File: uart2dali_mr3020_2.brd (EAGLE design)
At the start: 52 x 70 mm, 79 parts, among them IC2 LM393D, IC3 SFH6156, IC4 SFH6156, J1 AVR_SPI_PRG_6NS, Q1 SST201, Q2 BSP170P, Q3 BC817-25SMD, X1 SM04B-SRSS-TB

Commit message: - added values parts of constant current circuit - dali master can query from slaves
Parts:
- D5: value BZX84CSMD -> BZX84CSMD3v3
- D6: value BZX84CSMD -> BZX84CSMD12V
- R13: value (none) -> 3k9
- R14: value (none) -> 33k
- R15, R17, R18: value (none) -> 2k2
- R16: value (none) -> 1M
- R19: value (none) -> 1
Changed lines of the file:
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@@
 <element name="R3" library="resistor" package="R0603" value="27k" x="21.59" y="51.7525" rot="MR180"/>
 <element name="R4" library="resistor" package="R0603" value="82k" x="22.86" y="49.53" rot="MR0"/>
-<element name="R19" library="resistor" package="R0603" value="" x="15.5575" y="6.6675" rot="MR90"/>
+<element name="R19" library="resistor" package="R0603" value="1" x="15.5575" y="6.6675" rot="MR90"/>
 <element name="D7" library="diode" package="SMB" value="MBRS130LT3" x="30.48" y="18.7325" rot="MR0"/>
-<element name="R18" library="resistor" package="R0603" value="" x="36.5125" y="21.9075" rot="MR0"/>
-<element name="R13" library="resistor" package="R0603" value="" x="39.37" y="35.56" rot="MR90"/>
+<element name="R18" library="resistor" package="R0603" value="2k2" x="36.5125" y="21.9075" rot="MR0"/>
+<element name="R13" library="resistor" package="R0603" value="3k9" x="39.37" y="35.56" rot="MR90"/>
 <element name="C11" library="resistor" package="C0805" value="" x="35.2425" y="5.08" rot="MR270"/>
-<element name="R17" library="resistor" package="R0603" value="" x="27.94" y="23.495" rot="MR180"/>
-<element name="R16" library="resistor" package="R0603" value="" x="36.5125" y="25.7175" rot="MR0"/>
-<element name="D6" library="diode" package="TO236" value="BZX84CSMD" x="40.9575" y="26.3525" rot="MR0"/>
-<element name="R15" library="resistor" package="R0603" value="" x="32.0675" y="31.4325" rot="MR270"/>
-<element name="R14" library="resistor" package="R0603" value="" x="40.005" y="31.115" rot="MR270"/>
-<element name="D5" library="diode" package="TO236" value="BZX84CSMD" x="32.0675" y="22.86" rot="MR90"/>
+<element name="R17" library="resistor" package="R0603" value="2k2" x="27.94" y="23.495" rot="MR180"/>
+<element name="R16" library="resistor" package="R0603" value="1M" x="36.5125" y="25.7175" rot="MR0"/>
+<element name="D6" library="diode" package="TO236" value="BZX84CSMD12V" x="40.9575" y="26.3525" rot="MR0"/>
+<element name="R15" library="resistor" package="R0603" value="2k2" x="32.0675" y="31.4325" rot="MR270"/>
+<element name="R14" library="resistor" package="R0603" value="33k" x="40.005" y="31.115" rot="MR270"/>
+<element name="D5" library="diode" package="TO236" value="BZX84CSMD3v3" x="32.0675" y="22.86" rot="MR90"/>
 <element name="C10" library="resistor" package="C0603" value="" x="32.0675" y="35.56" rot="MR270"/>
 <element name="D8" library="diode" package="TO236" value="BZX84CSMD" x="39.37" y="4.445" rot="MR90"/>

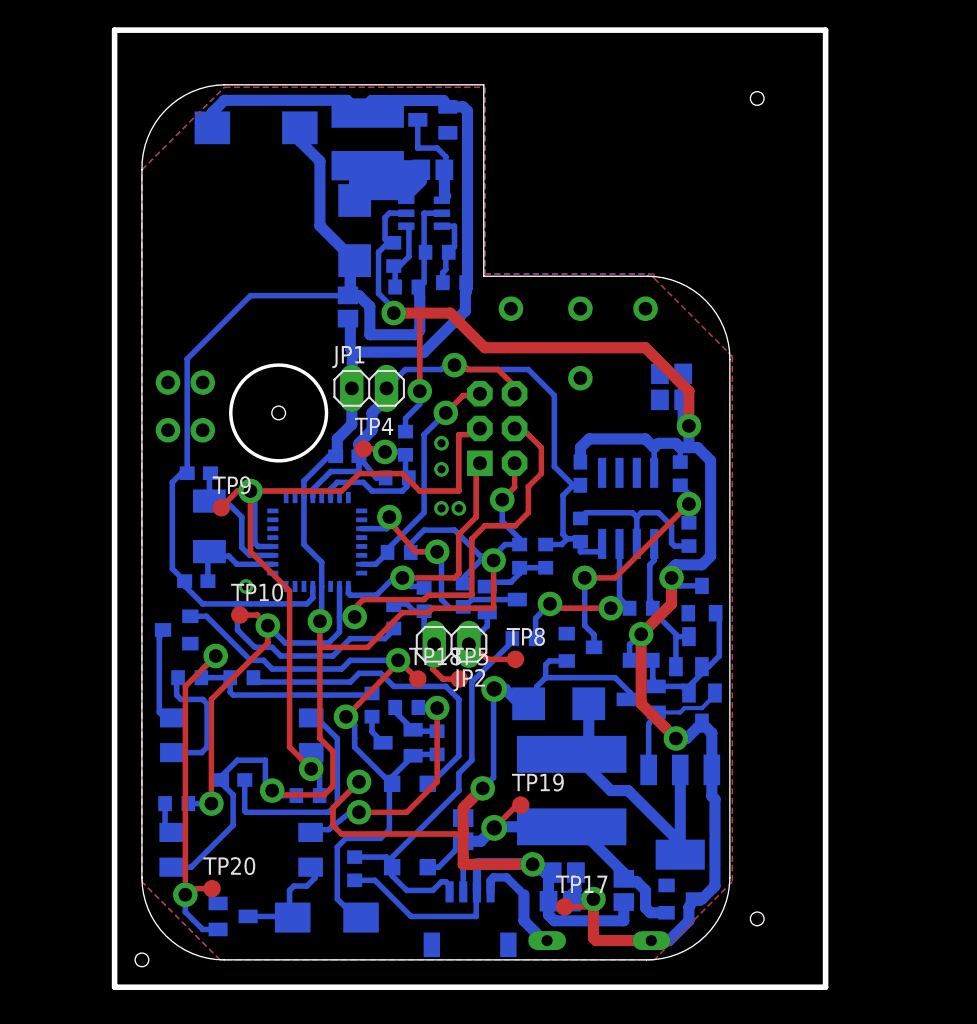
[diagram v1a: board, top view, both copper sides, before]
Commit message: got dali master firmware to a "working" state
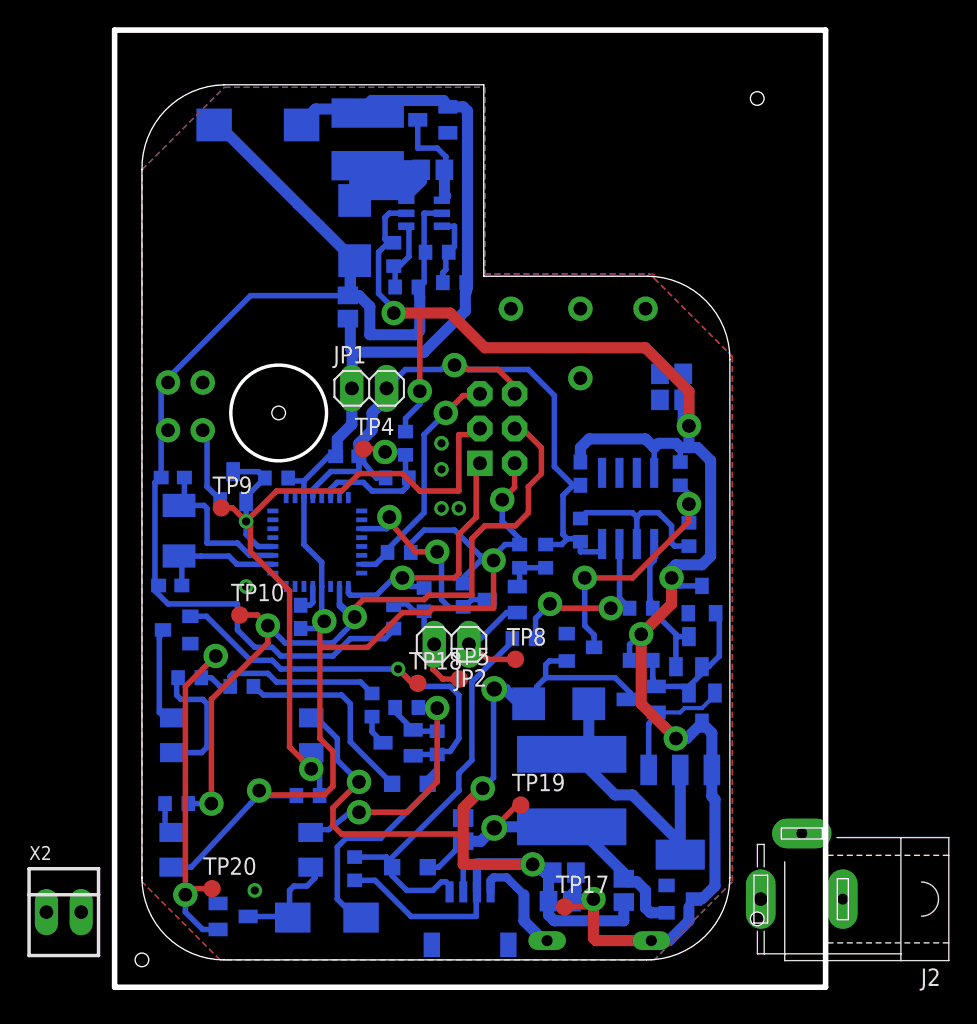
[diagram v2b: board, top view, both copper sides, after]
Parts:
- added J2: (no value), con-jack:SPC4078
- added R27: 10k, resistor:R0603
- added T4: (no value), transistor:SOT23-BEC
- added X2: 22-23-2021, con-molex:22-23-2021
- R10, R26, R7, R9: value (none) -> 10k
- R20: value (none) -> 1k2
- R21: value (none) -> 330
- R22: value (none) -> 3k
- R23: value (none) -> 0
- R25: value (none) -> 11k
- R5: value (none) -> 3k3
- R6, R8: value (none) -> 2k2
- T1: device transistor:SOT23-EBC -> transistor:SOT23-BEC
- moved C6 12.9 mm to (11.6, 25.1), turned to 270 degrees
- moved Y1 2.25 mm to (2.71, 31.4)
- moved C7 1.93 mm to (2.07, 27.4)
- moved C8 1.93 mm to (2.25, 35.3)
- moved R23 0.63 mm to (7.30, 20.0)
- moved TP18 0.32 mm to (20.2, 20.2)
- moved C5 0.25 mm to (8.48, 61.1), turned to 180 degrees
- turned T1 to 270 degrees
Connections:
- net +5V: now also R27.1
- net D+: now also B1.-; no longer B1.+
- net D-: now also B1.+; no longer B1.-
- net DALI_RCV: now also R27.2, T4.B, T4.C
- net GND: now also T4.E
- net VDD: no longer D8.C
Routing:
- net +5V: track 143.7 -> 134.7 mm
- net D-: track 23.5 -> 14.7 mm
- net GND: track 243.8 -> 238.2 mm, vias 17 -> 18
- net DALI_RCV: track 56.7 -> 59.4 mm
- net N$19: track 9.65 -> 12.1 mm
- net SOFT_RXD_5V: track 17.4 -> 15.2 mm
- net N$16: track 7.22 -> 9.35 mm
- net N$20: track 5.09 -> 3.35 mm
- net SOFT_RXD: track 6.66 -> 8.29 mm
- net VDD: track 130.5 -> 129.2 mm
- net DALI_TRM: track 55.7 -> 56.9 mm
- net N$35: track 18.2 -> 19.0 mm
- net D+: track 49.5 -> 48.9 mm, vias 2 -> 1
- net N$9: track 40.4 -> 40.9 mm
